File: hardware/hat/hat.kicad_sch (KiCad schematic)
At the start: 16 parts, among them J1 GPIO, J2 Uart, U1 CAT24C256, U2 TPS7A20xxxDBV, U3 Oled

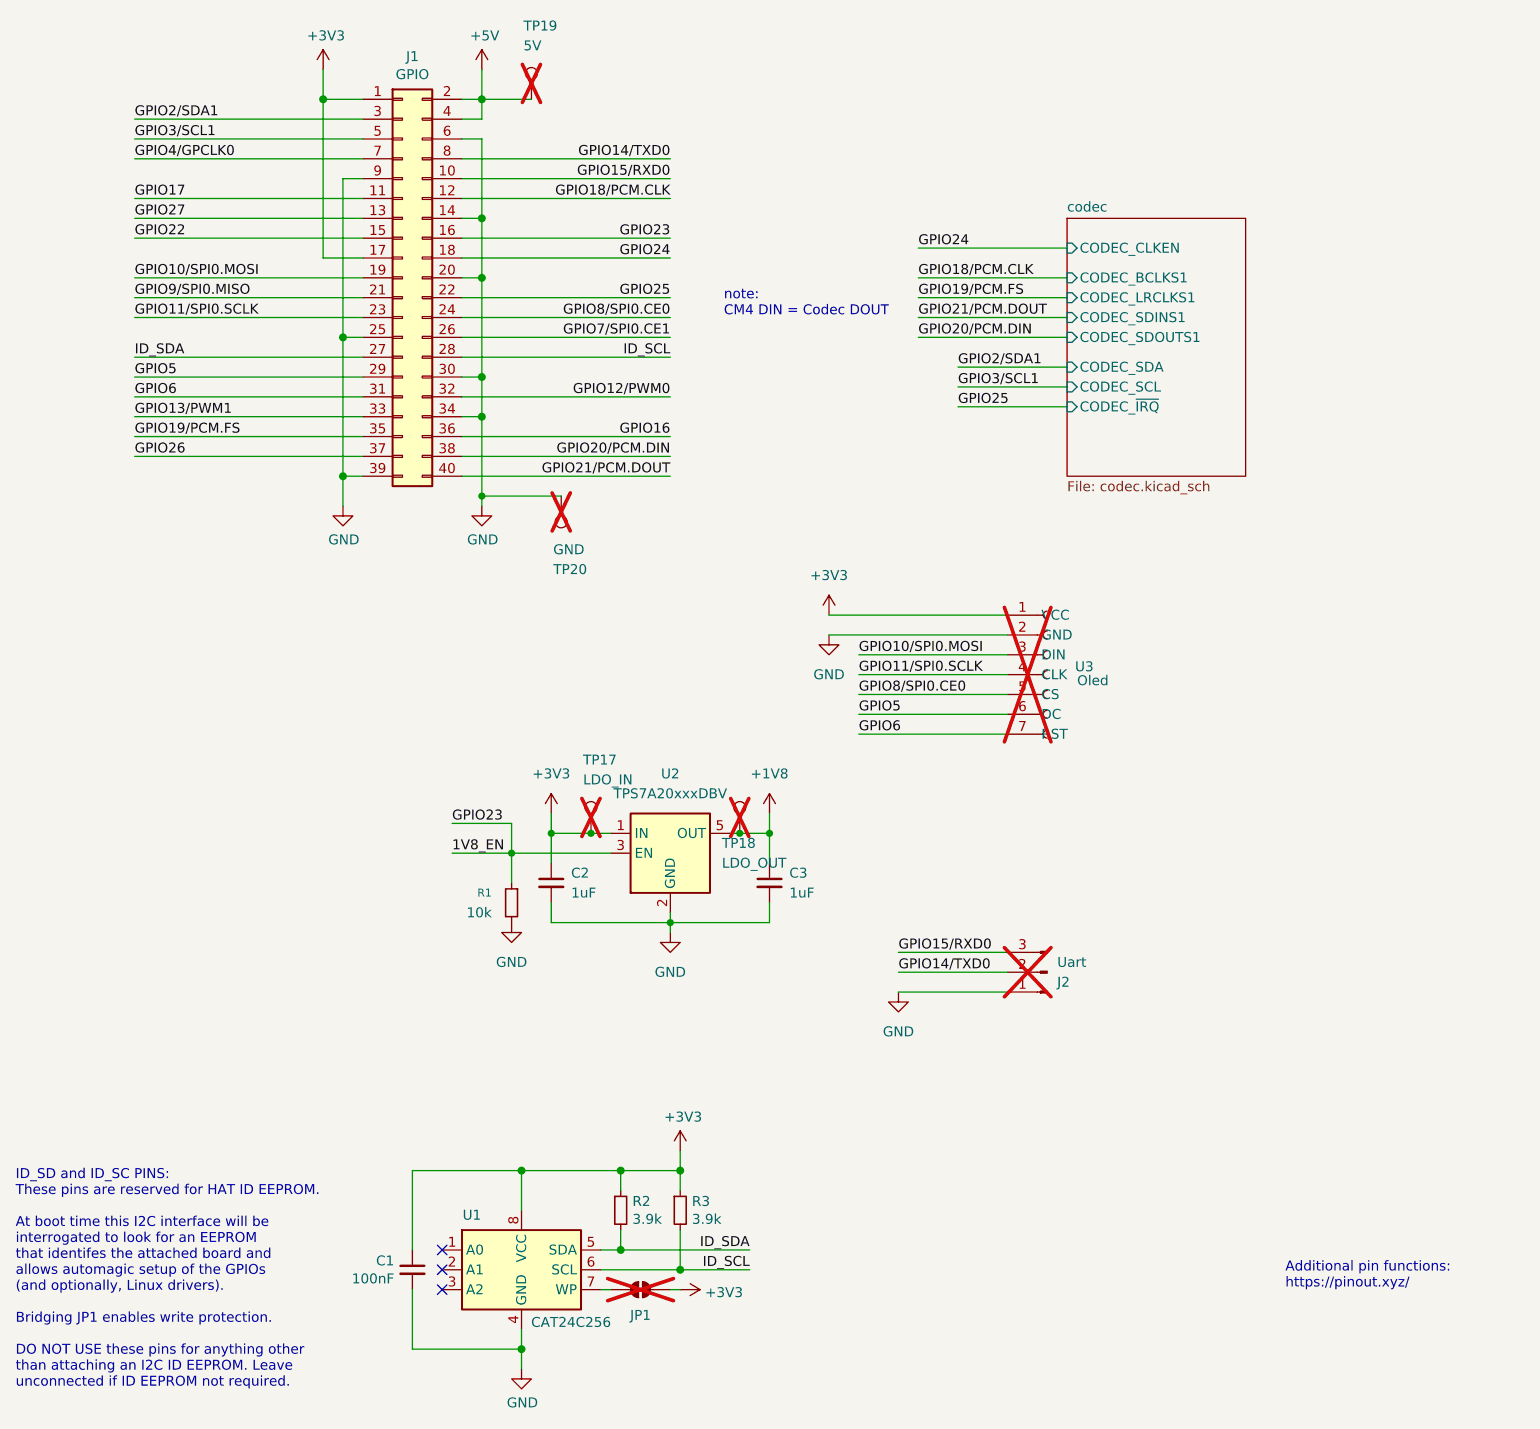
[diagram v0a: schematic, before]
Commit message: make hat 100 x sheetnum
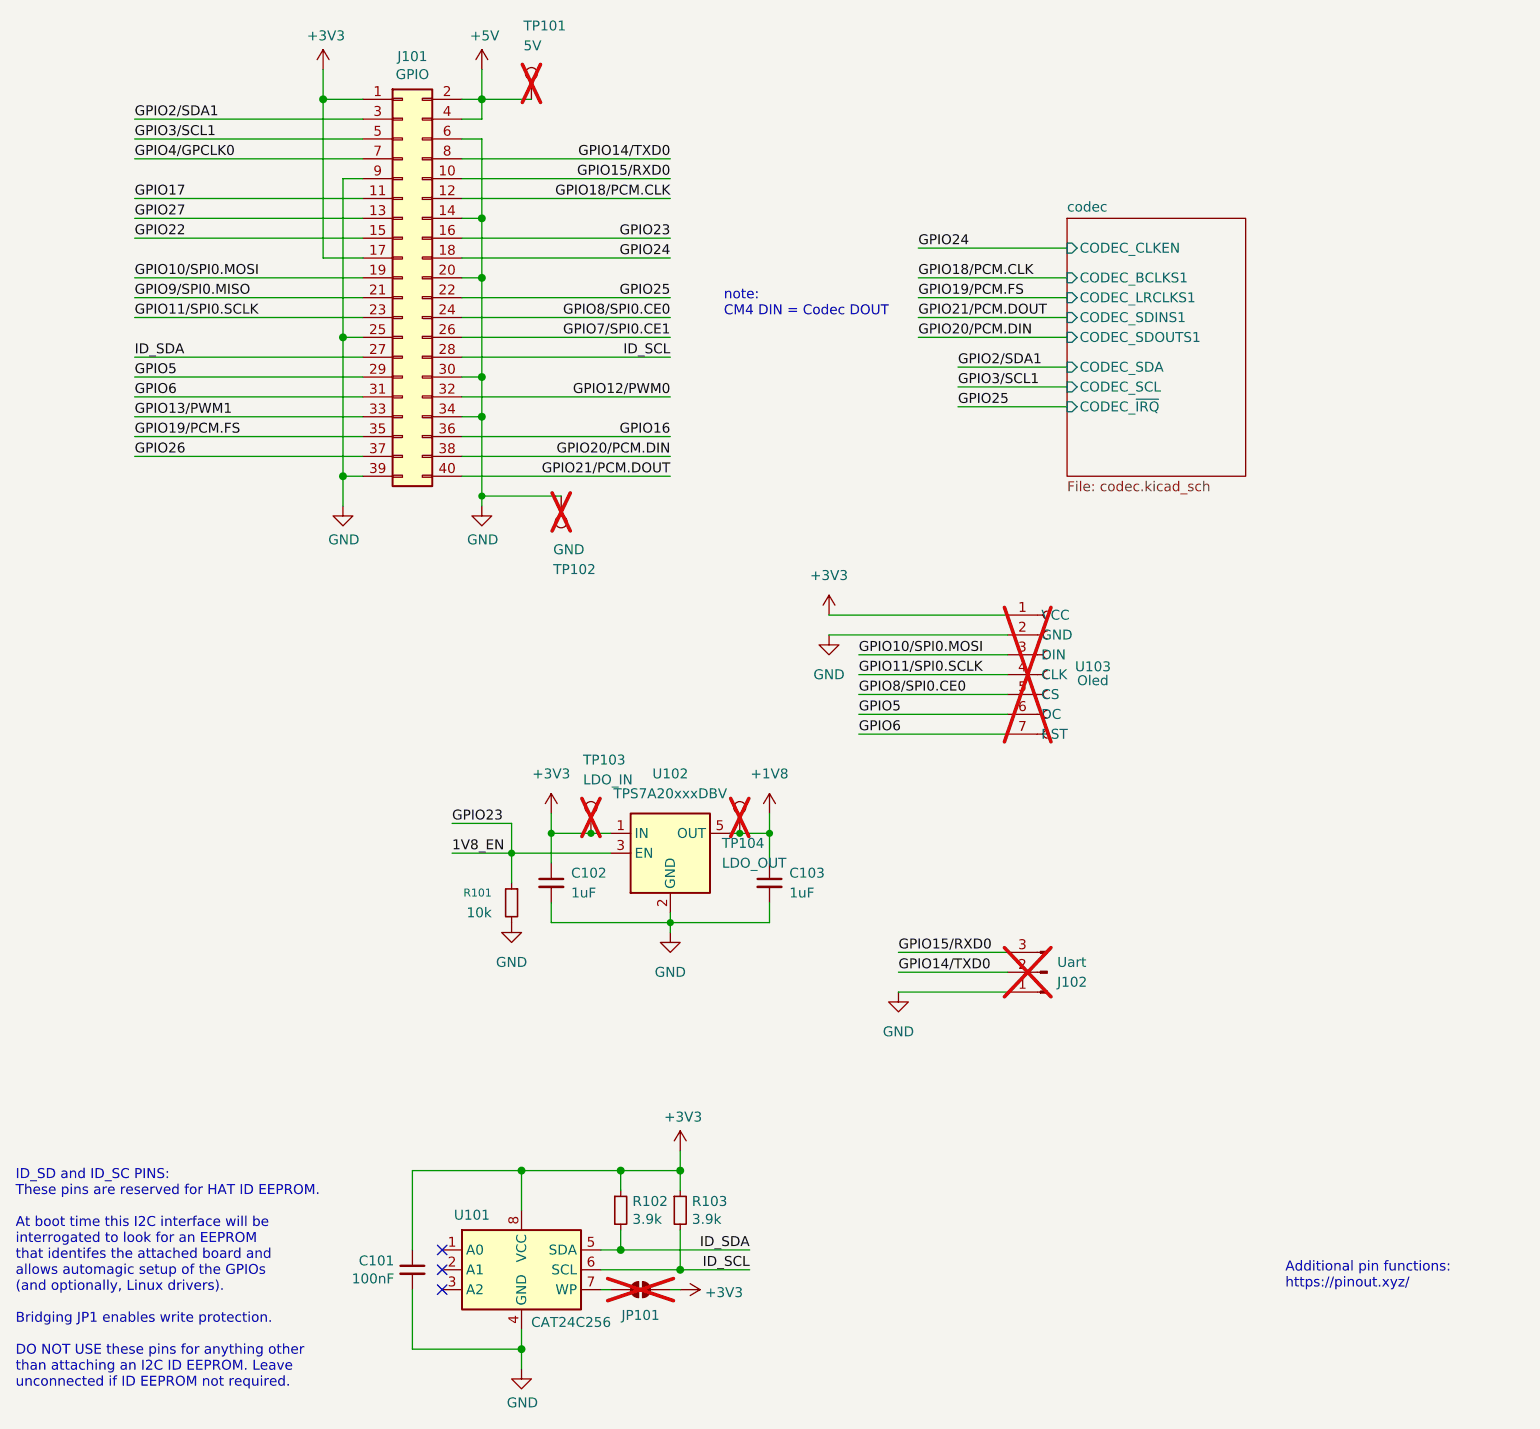
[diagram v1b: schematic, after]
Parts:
- renumbered C1 to C101, C2 to C102, C3 to C103, J1 to J101, J2 to J102, JP1 to JP101, R1 to R101, R2 to R102, R3 to R103, TP19 to TP101, TP20 to TP102, TP17 to TP103, TP18 to TP104, U1 to U101, U2 to U102, U3 to U103
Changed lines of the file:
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@@
 		(in_pos_files yes)
 		(dnp no)
-		(property "Reference" "#PWR03"
+		(property "Reference" "#PWR0103"
 			(at 76.2 27.94 0)
 			(hide yes)
@@
 			(project "hat"
 				(path "/e63e39d7-6ac0-4ffd-8aa3-1841a4541b55"
-					(reference "#PWR03")
+					(reference "#PWR0103")
 					(unit 1)
 				)
@@
 		(in_pos_files yes)
 		(dnp no)
-		(property "Reference" "#PWR01"
+		(property "Reference" "#PWR0101"
 			(at 55.88 27.94 0)
 			(hide yes)
@@
 			(project "hat"
 				(path "/e63e39d7-6ac0-4ffd-8aa3-1841a4541b55"
-					(reference "#PWR01")
+					(reference "#PWR0101")
 					(unit 1)
 				)
@@
 		(in_pos_files yes)
 		(dnp no)
-		(property "Reference" "#PWR04"
+		(property "Reference" "#PWR0104"
 			(at 76.2 86.36 0)
 			(hide yes)
@@
 			(project "hat"
 				(path "/e63e39d7-6ac0-4ffd-8aa3-1841a4541b55"
-					(reference "#PWR04")
+					(reference "#PWR0104")
 					(unit 1)
 				)
@@
 		(in_pos_files yes)
 		(dnp no)
-		(property "Reference" "#PWR02"
+		(property "Reference" "#PWR0102"
 			(at 58.42 86.36 0)
 			(hide yes)
@@
 			(project "hat"
 				(path "/e63e39d7-6ac0-4ffd-8aa3-1841a4541b55"
-					(reference "#PWR02")
+					(reference "#PWR0102")
 					(unit 1)
 				)
@@
 		(in_pos_files yes)
 		(dnp no)
-		(property "Reference" "J1"
+		(property "Reference" "J101"
 			(at 67.31 22.4598 0)
 			(show_name no)
@@
 			(project "hat"
 				(path "/e63e39d7-6ac0-4ffd-8aa3-1841a4541b55"
-					(reference "J1")
+					(reference "J101")
 					(unit 1)
 				)
@@
 		(dnp no)
 		(fields_autoplaced yes)
-		(property "Reference" "#PWR08"
+		(property "Reference" "#PWR0108"
 			(at 100.33 140.97 0)
 			(hide yes)
@@
 			(project "hat"
 				(path "/e63e39d7-6ac0-4ffd-8aa3-1841a4541b55"
-					(reference "#PWR08")
+					(reference "#PWR0108")
 					(unit 1)
 				)
@@
 		(in_pos_files yes)
 		(dnp no)
-		(property "Reference" "C1"
+		(property "Reference" "C101"
 			(at 64.9858 176.6506 0)
 			(show_name no)
@@
 			(project "hat"
 				(path "/e63e39d7-6ac0-4ffd-8aa3-1841a4541b55"
-					(reference "C1")
+					(reference "C101")
 					(unit 1)
 				)
@@
 		(in_pos_files yes)
 		(dnp no)
-		(property "Reference" "R2"
+		(property "Reference" "R102"
 			(at 95.4786 169.037 0)
 			(show_name no)
@@
 			(project "hat"
 				(path "/e63e39d7-6ac0-4ffd-8aa3-1841a4541b55"
-					(reference "R2")
+					(reference "R102")
 					(unit 1)
 				)
@@
 		(dnp no)
 		(fields_autoplaced yes)
-		(property "Reference" "#PWR07"
+		(property "Reference" "#PWR0107"
 			(at 85.09 123.19 0)
 			(hide yes)
@@
 			(project "hat"
 				(path "/e63e39d7-6ac0-4ffd-8aa3-1841a4541b55"
-					(reference "#PWR07")
+					(reference "#PWR0107")
 					(unit 1)
 				)
@@
 		(dnp no)
 		(fields_autoplaced yes)
-		(property "Reference" "U2"
+		(property "Reference" "U102"
 			(at 100.33 114.3 0)
 			(show_name no)
@@
 			(project "hat"
 				(path "/e63e39d7-6ac0-4ffd-8aa3-1841a4541b55"
-					(reference "U2")
+					(reference "U102")
 					(unit 1)
 				)
@@
 		(in_pos_files yes)
 		(dnp yes)
-		(property "Reference" "TP20"
+		(property "Reference" "TP102"
 			(at 85.344 88.138 0)
 			(show_name no)
@@
 			(project "hat"
 				(path "/e63e39d7-6ac0-4ffd-8aa3-1841a4541b55"
-					(reference "TP20")
+					(reference "TP102")
 					(unit 1)
 				)
@@
 		(in_pos_files yes)
 		(dnp yes)
-		(property "Reference" "J2"
+		(property "Reference" "J102"
 			(at 149.86 140.9701 0)
 			(show_name no)
@@
 			(project "hat"
 				(path "/e63e39d7-6ac0-4ffd-8aa3-1841a4541b55"
-					(reference "J2")
+					(reference "J102")
 					(unit 1)
 				)
@@
 		(in_pos_files yes)
 		(dnp yes)
-		(property "Reference" "JP1"
+		(property "Reference" "JP101"
 			(at 96.52 183.623 0)
 			(show_name no)
@@
 			(project "hat"
 				(path "/e63e39d7-6ac0-4ffd-8aa3-1841a4541b55"
-					(reference "JP1")
+					(reference "JP101")
 					(unit 1)
 				)
@@
 		(in_pos_files yes)
 		(dnp no)
-		(property "Reference" "R3"
+		(property "Reference" "R103"
 			(at 103.0986 169.037 0)
 			(show_name no)
@@
 			(project "hat"
 				(path "/e63e39d7-6ac0-4ffd-8aa3-1841a4541b55"
-					(reference "R3")
+					(reference "R103")
 					(unit 1)
 				)
@@
 		(in_pos_files yes)
 		(dnp no)
-		(property "Reference" "#PWR09"
+		(property "Reference" "#PWR0109"
 			(at 101.6 166.37 0)
 			(hide yes)
@@
 			(project "hat"
 				(path "/e63e39d7-6ac0-4ffd-8aa3-1841a4541b55"
-					(reference "#PWR09")
+					(reference "#PWR0109")
 					(unit 1)
 				)
@@
 		(in_pos_files yes)
 		(dnp yes)
-		(property "Reference" "U3"
+		(property "Reference" "U103"
 			(at 152.146 100.584 0)
 			(show_name no)
@@
 			(project "hat"
 				(path "/e63e39d7-6ac0-4ffd-8aa3-1841a4541b55"
-					(reference "U3")
+					(reference "U103")
 					(unit 1)
 				)
@@
 		(dnp no)
 		(fields_autoplaced yes)
-		(property "Reference" "#PWR013"
+		(property "Reference" "#PWR0113"
 			(at 120.65 102.87 0)
 			(hide yes)
@@
 			(project "hat"
 				(path "/e63e39d7-6ac0-4ffd-8aa3-1841a4541b55"
-					(reference "#PWR013")
+					(reference "#PWR0113")
 					(unit 1)
 				)
@@
 		(dnp no)
 		(fields_autoplaced yes)
-		(property "Reference" "C3"
+		(property "Reference" "C103"
 			(at 115.57 127.0062 0)
 			(show_name no)
@@
 			(project "hat"
 				(path "/e63e39d7-6ac0-4ffd-8aa3-1841a4541b55"
-					(reference "C3")
+					(reference "C103")
 					(unit 1)
 				)
@@
 		(in_pos_files yes)
 		(dnp no)
-		(property "Reference" "U1"
+		(property "Reference" "U101"
 			(at 74.93 170.7958 0)
 			(show_name no)
@@
 			(project "hat"
 				(path "/e63e39d7-6ac0-4ffd-8aa3-1841a4541b55"
-					(reference "U1")
+					(reference "U101")
 					(unit 1)
 				)
@@
 		(in_pos_files yes)
 		(dnp no)
-		(property "Reference" "#PWR014"
+		(property "Reference" "#PWR0114"
 			(at 129.54 148.59 0)
 			(hide yes)
@@
 			(project "hat"
 				(path "/e63e39d7-6ac0-4ffd-8aa3-1841a4541b55"
-					(reference "#PWR014")
+					(reference "#PWR0114")
 					(unit 1)
 				)
@@
 		(dnp no)
 		(fields_autoplaced yes)
-		(property "Reference" "#PWR011"
+		(property "Reference" "#PWR0111"
 			(at 113.03 123.19 0)
 			(hide yes)
@@
 			(project "hat"
 				(path "/e63e39d7-6ac0-4ffd-8aa3-1841a4541b55"
-					(reference "#PWR011")
+					(reference "#PWR0111")
 					(unit 1)
 				)
@@
 		(in_pos_files yes)
 		(dnp yes)
-		(property "Reference" "TP19"
+		(property "Reference" "TP101"
 			(at 81.534 18.542 0)
 			(show_name no)
@@
 			(project "hat"
 				(path "/e63e39d7-6ac0-4ffd-8aa3-1841a4541b55"
-					(reference "TP19")
+					(reference "TP101")
 					(unit 1)
 				)
@@
 		(dnp no)
 		(fields_autoplaced yes)
-		(property "Reference" "#PWR012"
+		(property "Reference" "#PWR0112"
 			(at 120.65 97.79 0)
 			(hide yes)
@@
 			(project "hat"
 				(path "/e63e39d7-6ac0-4ffd-8aa3-1841a4541b55"
-					(reference "#PWR012")
+					(reference "#PWR0112")
 					(unit 1)
 				)
@@
 		(in_pos_files yes)
 		(dnp no)
-		(property "Reference" "#PWR06"
+		(property "Reference" "#PWR0106"
 			(at 81.28 196.85 0)
 			(hide yes)
@@
 			(project "hat"
 				(path "/e63e39d7-6ac0-4ffd-8aa3-1841a4541b55"
-					(reference "#PWR06")
+					(reference "#PWR0106")
 					(unit 1)
 				)
@@
 		(in_pos_files yes)
 		(dnp yes)
-		(property "Reference" "TP17"
+		(property "Reference" "TP103"
 			(at 89.154 112.522 0)
 			(show_name no)
@@
 			(project "hat"
 				(path "/e63e39d7-6ac0-4ffd-8aa3-1841a4541b55"
-					(reference "TP17")
+					(reference "TP103")
 					(unit 1)
 				)
@@
 		(in_pos_files yes)
 		(dnp no)
-		(property "Reference" "R1"
+		(property "Reference" "R101"
 			(at 77.47 129.5399 0)
 			(show_name no)
@@
 			(project "hat"
 				(path "/e63e39d7-6ac0-4ffd-8aa3-1841a4541b55"
-					(reference "R1")
+					(reference "R101")
 					(unit 1)
 				)
@@
 		(in_pos_files yes)
 		(dnp no)
-		(property "Reference" "#PWR010"
+		(property "Reference" "#PWR0110"
 			(at 97.79 180.34 0)
 			(hide yes)
@@
 			(project "hat"
 				(path "/e63e39d7-6ac0-4ffd-8aa3-1841a4541b55"
-					(reference "#PWR010")
+					(reference "#PWR0110")
 					(unit 1)
 				)
@@
 		(in_pos_files yes)
 		(dnp yes)
-		(property "Reference" "TP18"
+		(property "Reference" "TP104"
 			(at 106.934 123.19 0)
 			(show_name no)
@@
 			(project "hat"
 				(path "/e63e39d7-6ac0-4ffd-8aa3-1841a4541b55"
-					(reference "TP18")
+					(reference "TP104")
 					(unit 1)
 				)
@@
 		(dnp no)
 		(fields_autoplaced yes)
-		(property "Reference" "#PWR05"
+		(property "Reference" "#PWR0105"
 			(at 80.01 139.7 0)
 			(hide yes)
@@
 			(project "hat"
 				(path "/e63e39d7-6ac0-4ffd-8aa3-1841a4541b55"
-					(reference "#PWR05")
+					(reference "#PWR0105")
 					(unit 1)
 				)
@@
 		(dnp no)
 		(fields_autoplaced yes)
-		(property "Reference" "C2"
+		(property "Reference" "C102"
 			(at 87.63 127.0062 0)
 			(show_name no)
@@
 			(project "hat"
 				(path "/e63e39d7-6ac0-4ffd-8aa3-1841a4541b55"
-					(reference "C2")
-					(unit 1)
-				)
+					(reference "C102")
+					(unit 1)
+				)
